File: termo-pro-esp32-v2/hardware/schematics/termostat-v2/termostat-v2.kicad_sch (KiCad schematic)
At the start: 13 parts, among them Q2 PN2222A, SW1 SW_Push, SW2 SW_Push, SW3 SW_Push, SW4 SW_Push, U1 ESP32-DevKitC, U2 DHT11

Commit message: schematic redone and improvment.
more to come...
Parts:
- added C2, C3: 50V 220nF, Capacitor_THT:C_Radial_D10.0mm_H12.5mm_P5.00mm, symbol Device:C
- C1: footprint (none) -> Capacitor_THT:CP_Radial_D8.0mm_P5.00mm
- R1: footprint (none) -> OptoDevice:R_LDR_5.0x4.1mm_P3mm_Vertical
- R2, R7: footprint (none) -> Resistor_THT:R_Axial_DIN0207_L6.3mm_D2.5mm_P7.62mm_Horizontal
- RV3: footprint (none) -> Potentiometer_THT:Potentiometer_Runtron_RM-065_Vertical
- SW1, SW2, SW3, SW4: footprint (none) -> Button_Switch_THT:SW_PUSH_6mm
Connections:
- net +VDC: now also C2.2, C3.2
- net -VDC: now also C2.1, C3.1
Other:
- moved on the sheet: C1, R1, U2

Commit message: *
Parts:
- R7: value 1k -> 330
- U1: value ESP32-DevKitC -> ESP32-DevKitM; footprint PCM_Espressif:ESP32-DevKitC -> (none)
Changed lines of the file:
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@@
 		(dnp no)
 		(property "Reference" "R7"
-			(at 85.09 83.82 90)
-			(show_name no)
-			(do_not_autoplace no)
-			(effects
-				(font
-					(size 1.27 1.27)
-				)
-			)
-		)
-		(property "Value" "1k"
-			(at 88.138 83.82 90)
+			(at 87.63 84.074 90)
+			(show_name no)
+			(do_not_autoplace no)
+			(effects
+				(font
+					(size 1.27 1.27)
+				)
+			)
+		)
+		(property "Value" "330"
+			(at 87.63 88.646 90)
 			(show_name no)
 			(do_not_autoplace no)
@@
 		(dnp no)
 		(property "Reference" "U1"
-			(at 116.84 110.49 90)
-			(show_name no)
-			(do_not_autoplace no)
-			(effects
-				(font
-					(size 1.27 1.27)
-				)
-			)
-		)
-		(property "Value" "ESP32-DevKitC"
-			(at 119.38 110.49 90)
-			(show_name no)
-			(do_not_autoplace no)
-			(effects
-				(font
-					(size 1.27 1.27)
-				)
-			)
-		)
-		(property "Footprint" "PCM_Espressif:ESP32-DevKitC"
+			(at 122.174 105.156 90)
+			(show_name no)
+			(do_not_autoplace no)
+			(effects
+				(font
+					(size 1.27 1.27)
+				)
+			)
+		)
+		(property "Value" "ESP32-DevKitM"
+			(at 125.476 104.902 90)
+			(show_name no)
+			(do_not_autoplace no)
+			(effects
+				(font
+					(size 1.27 1.27)
+				)
+			)
+		)
+		(property "Footprint" ""
 			(at 142.24 135.89 0)
 			(hide yes)
@@
 			)
 		)
-		(property "Datasheet" "https://docs.espressif.com/projects/esp-idf/zh_CN/latest/esp32/hw-reference/esp32/get-started-devkitc.html"
+		(property "Datasheet" ""
 			(at 142.24 138.43 0)
 			(hide yes)
@@
 			)
 		)
-		(property "Description" "Development Kit"
+		(property "Description" ""
 			(at 142.24 92.71 0)
 			(hide yes)

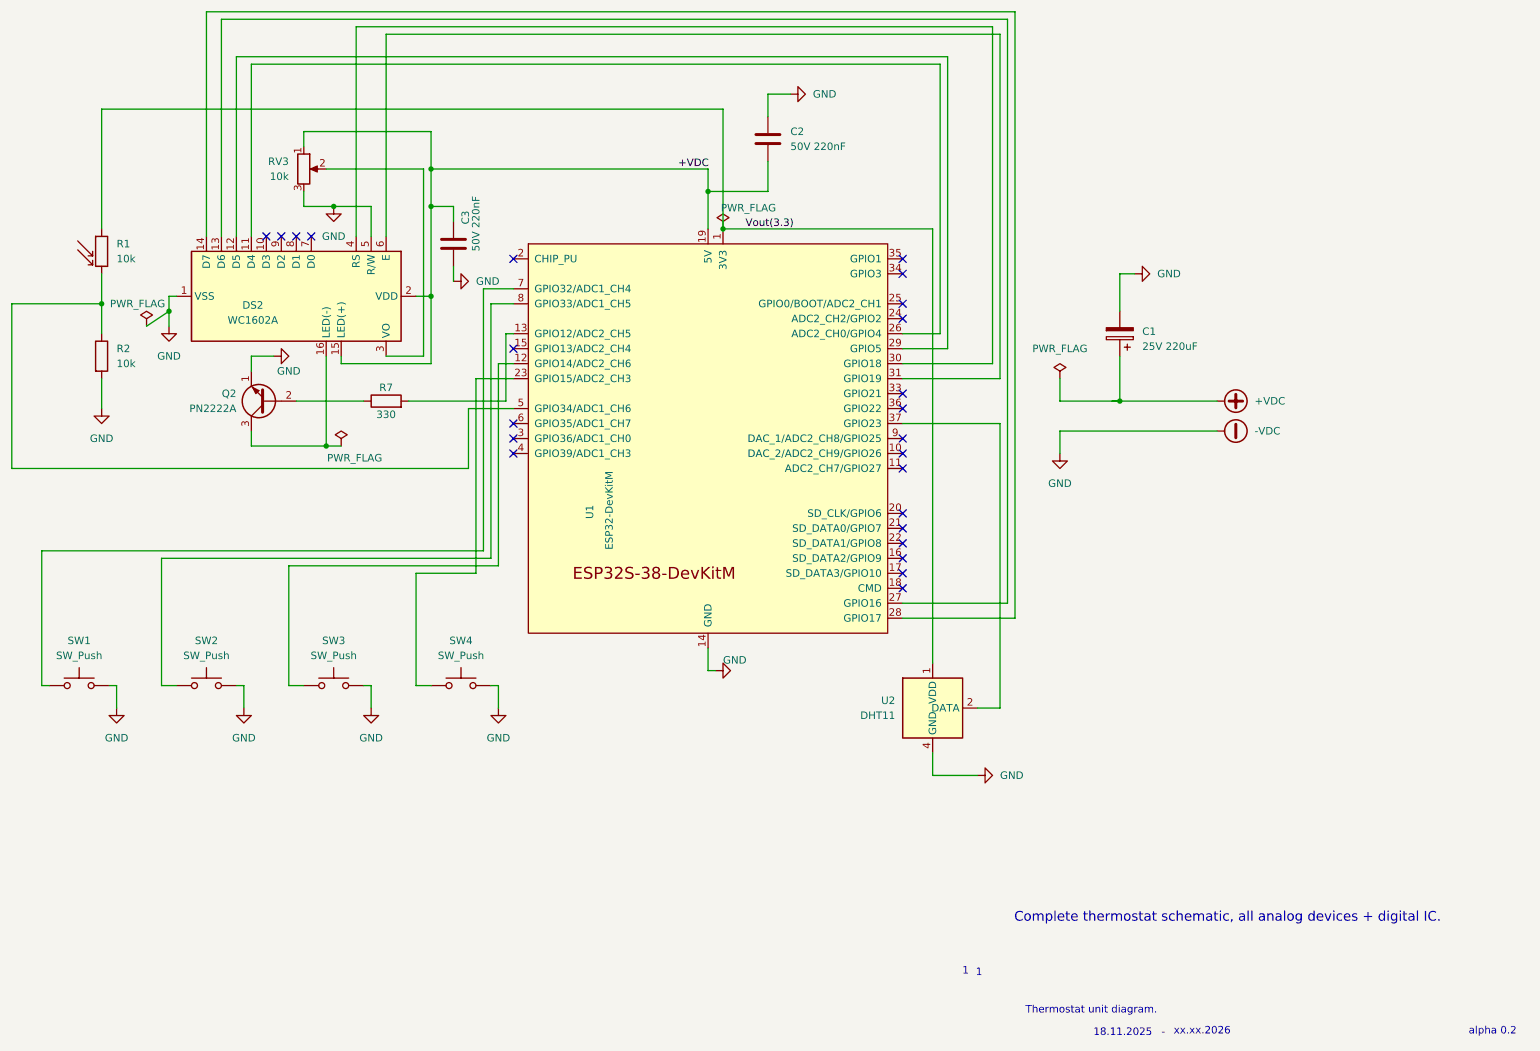
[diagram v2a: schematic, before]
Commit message: Firmware modification and complete schematics redone and improvement.
All schematics have been redone.
All components have footprints.
Microcontrollers  used ESP32S-38 NodeMCU and ESP32-C3-SuperMini.

ESP8266 has been eliminated because of compatibility issues.

Next phase is PCB design.
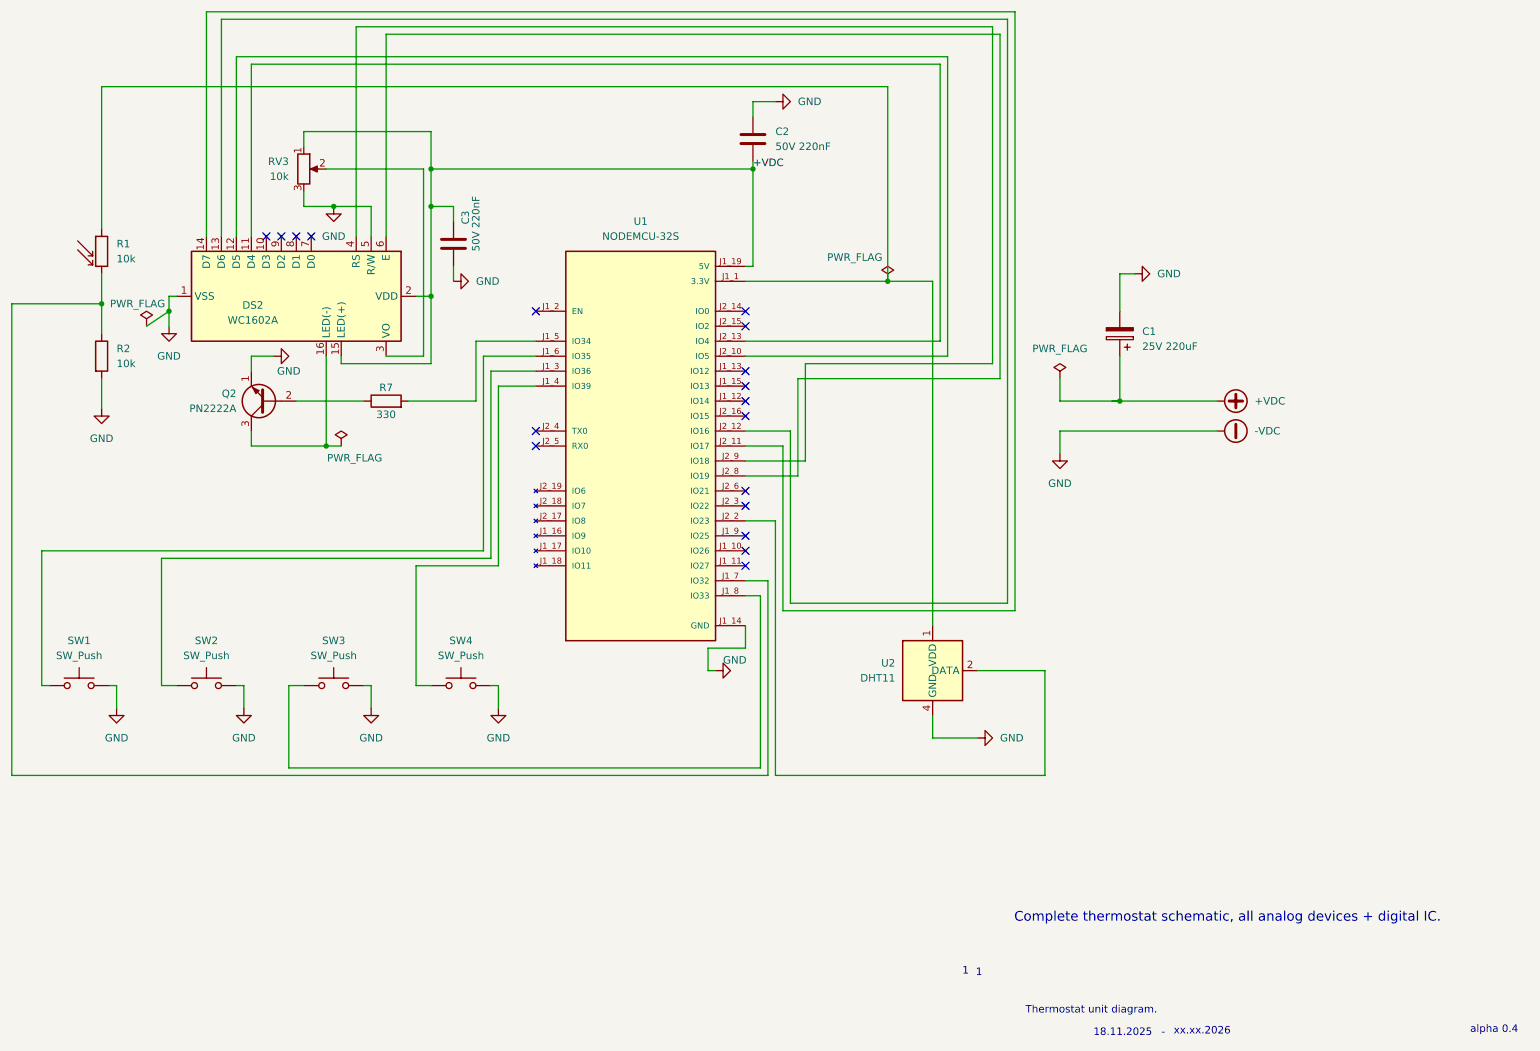
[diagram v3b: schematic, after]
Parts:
- removed U1: ESP32-DevKitM, symbol ESP32-All:ESP32-DevKitC
- added U1: NODEMCU-32S, NODEMCU-ESP32S:MODULE_NODEMCU-32S, symbol NODEMCU-32S:NODEMCU-32S
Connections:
- net +VDC: now also U1.J1_19 (5V)
- net -VDC: now also U1.J1_14 (GND), U1.J2_1 (GND), U1.J2_7 (GND)
- net at R7.2: now also U1.J1_5 (IO34)
- net at SW1.1: now also U1.J1_6 (IO35)
- net at U2.2 (DATA): now also U1.J2_2 (IO23)
- net at SW2.1: now also U1.J1_3 (IO36)
- net at SW4.1: now also U1.J1_4 (IO39)
- net at SW3.1: now also U1.J1_8 (IO33)
- net at DS2.11 (D4): now also U1.J2_13 (IO4)
- net at DS2.12 (D5): now also U1.J2_10 (IO5)
- net at DS2.13 (D6): now also U1.J2_12 (IO16)
- net at DS2.14 (D7): now also U1.J2_11 (IO17)
- net at DS2.4 (RS): now also U1.J2_9 (IO18)
- net at DS2.6 (E): now also U1.J2_8 (IO19)
- net at R1.2, R2.1: now also U1.J1_7 (IO32)
- net Vout(3.3): no longer names the net of R1.1, U2.1 (VDD)
- net Vout(3.3): now also U1.J1_1 (3.3V)
- no-connect marks 24 -> 18
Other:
- note added: "alpha 0.4"
- note removed: "alpha 0.2"
- moved on the sheet: C2, U2
